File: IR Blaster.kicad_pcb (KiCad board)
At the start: 2 copper layers, 47.8 x 35.8 mm, 54 parts, among them CON1 AVR-ISP-6, IC1 ATMEGA328P-A, P1 FTDI Header, P2 IR Receiver, P3 Analog IN, P4 PWR, Q1 FDV303N, U1 ATSHA204A, U2 NRF24L01, U3 AT25DF512C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

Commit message: Updated revision from v0.4 to v0.5 for first board run.
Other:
- board text added: "MySensors.org IR Blaster Version 0.5"
- board text removed: "MySensors.org IR Blaster Version 0.4"

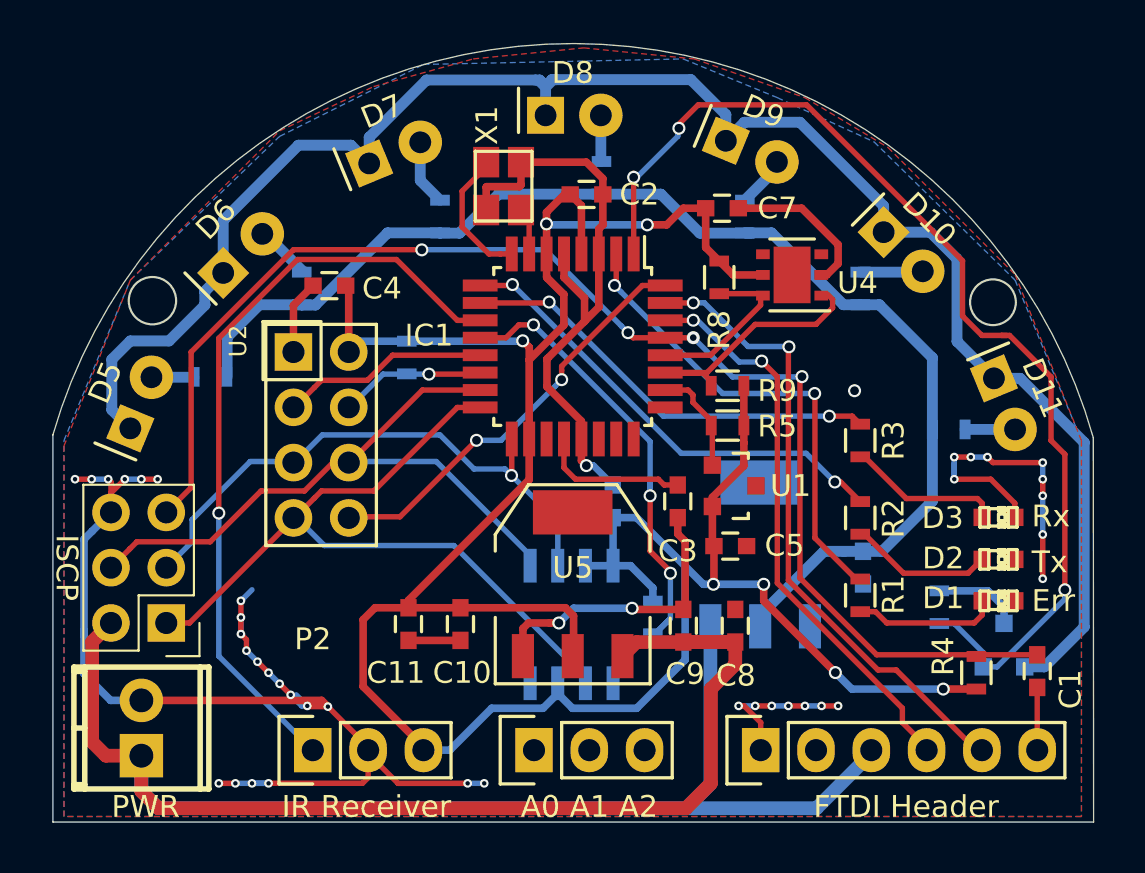
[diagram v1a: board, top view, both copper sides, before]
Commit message: Resolved fab house design requirement violations.  "Stitched" vias exceeded minimum drill size for fab house and wider pwr traces were closer to the edge than the minimum allow.
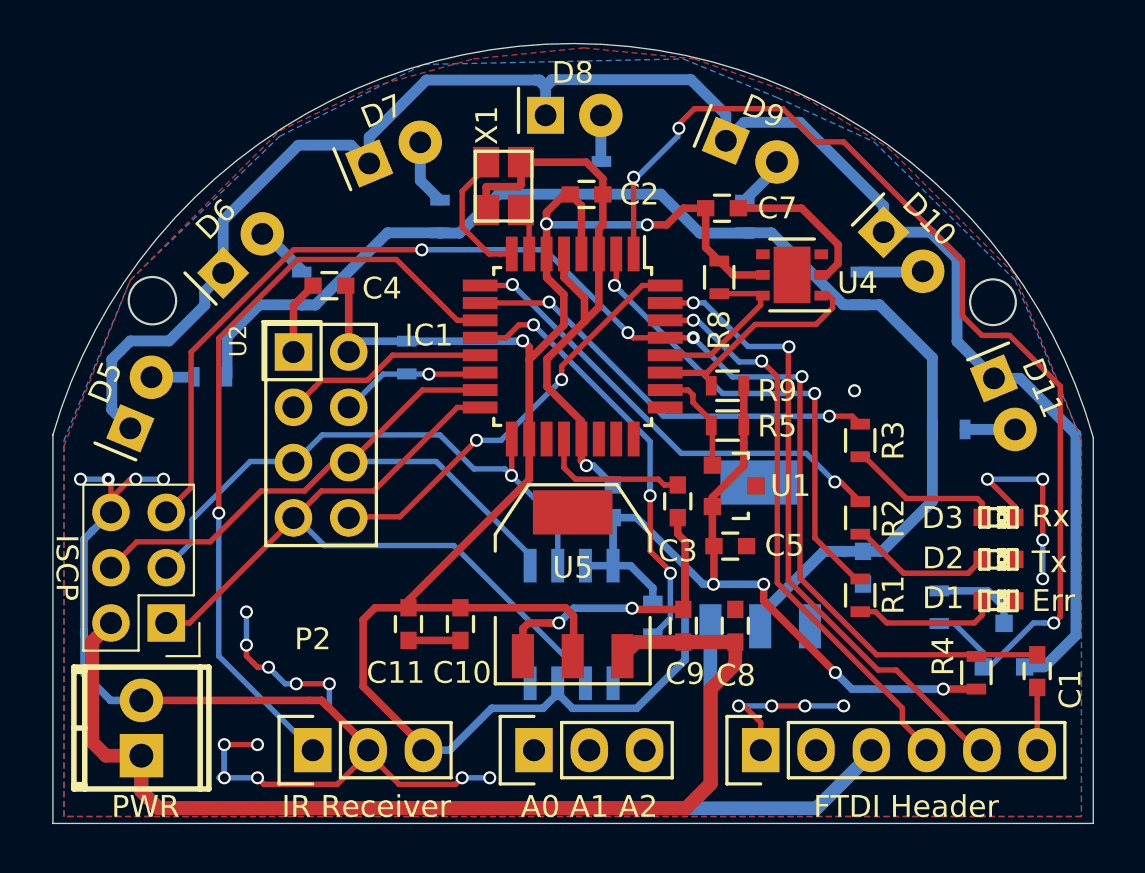
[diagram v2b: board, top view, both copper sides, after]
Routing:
- net GND: track 136.8 -> 135.7 mm, vias 41 -> 26
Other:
- rule via_min_drill: 0.3 -> 0.33
